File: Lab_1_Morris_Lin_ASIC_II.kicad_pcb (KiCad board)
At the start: 4 copper layers, 100 x 100 mm, 100 parts, among them IC1 74CBTLV3253D,118, IC2 74CBTLV3253D,118, IC3 74CBTLV3253D,118, IC4 74CBTLV3253D,118, IC5 74CBTLV3253D,118, IC6 74CBTLV3253D,118, J1 VDDPST_External, J10 Conn_01x14, J11 Conn_01x14, J2 PMOD_A, J3 PMOD_B, J4 VDD_Qn External, J5 VDDPST External, J6 PMOD_A, J7 PMOD_B, J8 Conn_01x14, J9 Conn_01x14, Q1 BSS138, U1 TLV75710PDBV, U2 TLV75710PDBV

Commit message: blank for run
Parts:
- removed J1: VDDPST_External, Connector:Banana_Jack_2Pin
- added J12: VDDPST External, Connector:Banana_Jack_1Pin, F.Cu at (47.8, 111.1)
- added J13: GND External, Connector:Banana_Jack_1Pin, F.Cu at (47.7, 125.5)
- IC1, IC2, IC3: moved to F.Cu
- J5: value VDDPST External -> VDDRING External
- moved JP5 76.2 mm to (44.9, 53.7), turned to 0 degrees
- moved JP9 69.5 mm to (50.4, 53.7), turned to 0 degrees
- moved R5 66.3 mm to (44.6, 69.5), turned to -90 degrees
- moved JP6 64.6 mm to (45.2, 63.9), turned to 90 degrees
- moved R6 58.4 mm to (44.6, 76.2), turned to 90 degrees
- moved IC2 58.3 mm to (61.0, 60.6), turned to 180 degrees
- moved R8 49.3 mm to (49.6, 79.2), turned to 0 degrees
- moved D7 48.9 mm to (49.7, 74.8)
- moved R10 48.0 mm to (48.8, 69.5), turned to -90 degrees
- moved IC4 44.4 mm to (118.7, 60.6), turned to 180 degrees
- moved Q1 34.0 mm to (117.9, 102.3), turned to 0 degrees
- moved D6 33.2 mm to (117.5, 107.7), turned to -90 degrees
- moved JP1 30.8 mm to (50.5, 102.5)
- moved TP6 30.8 mm to (44.1, 82.3)
- moved C5 30.8 mm to (49.7, 92.9)
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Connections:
- J2 pad 12: VDDPMOD -> unconnected-(J2-Pin_12-Pad12)
- J3 pad 12: VDDPMOD -> unconnected-(J3-Pin_12-Pad12)
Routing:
- net VDDPMOD: track 0.00 -> 96.4 mm
- net VDD: track 40.6 -> 136.5 mm
- net VDDPST: track 17.0 -> 64.4 mm, vias 14 -> 18
- net Net-(JP10-A): track 0.00 -> 46.9 mm
- net VDD_Q1: track 16.8 -> 61.8 mm
- net VDD_Q3: track 17.3 -> 59.8 mm
- net VDD_Q4: track 16.4 -> 58.1 mm
- net VDD_Q2: track 17.0 -> 55.3 mm
- net /LED_Q4: track 0.00 -> 23.7 mm
- net GND: track 0.00 -> 21.1 mm, vias 0 -> 5
- net /LED_Q3: track 0.00 -> 17.9 mm
- net Net-(JP2-B): track 0.00 -> 15.9 mm
- net /SEL_b0: track 0.00 -> 13.6 mm
- net Net-(J5-Pin_1): track 0.00 -> 12.5 mm
- net /SEL_b1: track 0.00 -> 12.4 mm
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- removed copper zone on F.Cu, net Net-(J5-Pin_1)

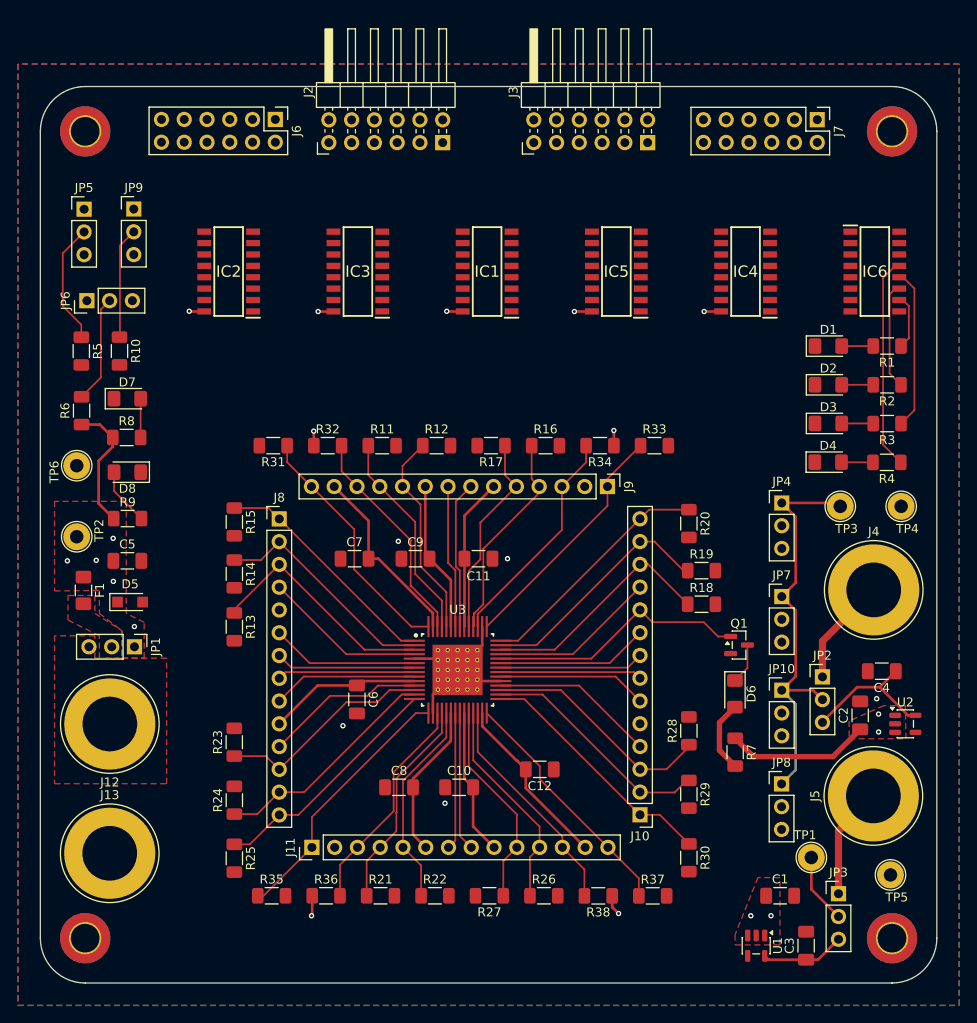
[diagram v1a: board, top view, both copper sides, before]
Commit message: Routing done, pesky GND zone error remains
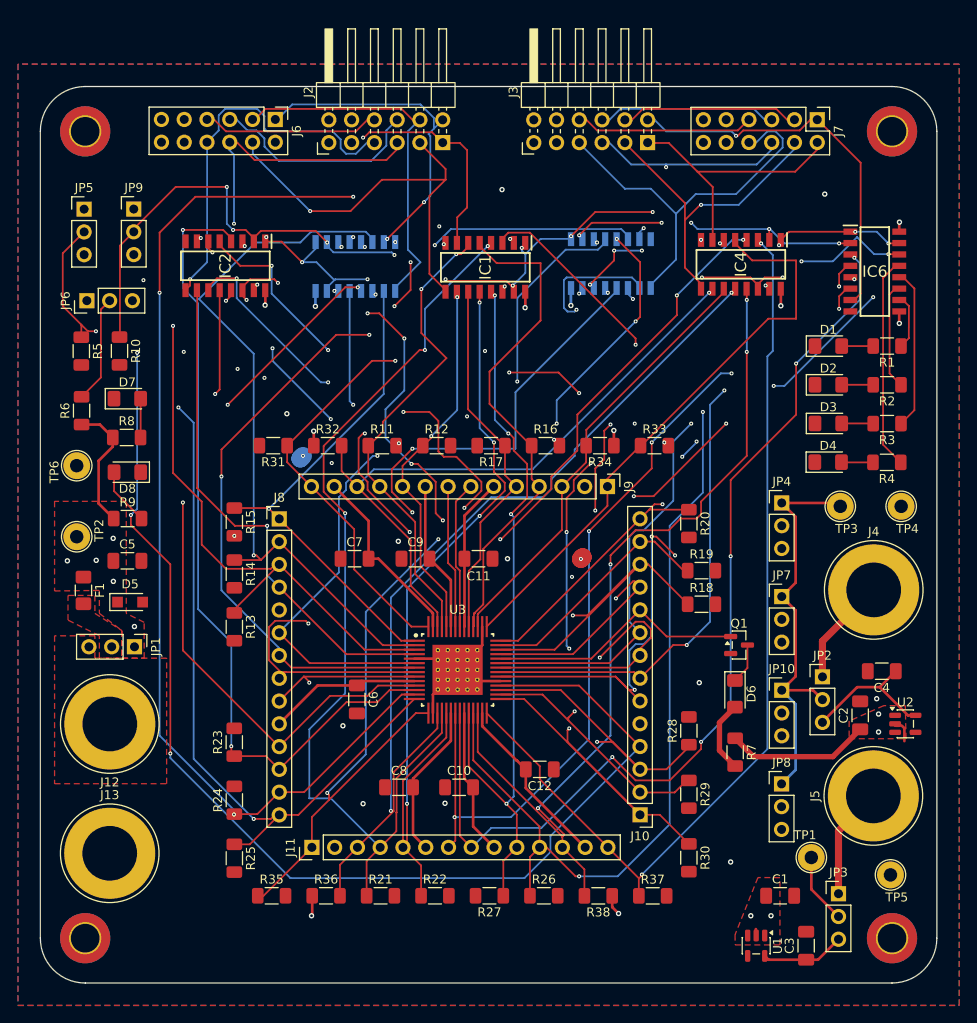
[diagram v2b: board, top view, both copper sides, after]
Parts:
- IC3, IC5: moved to B.Cu
- moved IC5 1.08 mm to (103.6, 59.8), turned to -90 degrees
- moved IC4 0.96 mm to (118.1, 59.8), turned to -90 degrees
- moved IC2 0.74 mm to (60.6, 60.0), turned to -90 degrees
- moved IC3 0.63 mm to (75.1, 60.1), turned to -90 degrees
- moved IC1 0.51 mm to (89.6, 60.2), turned to -90 degrees
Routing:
- net /~{OE}: track 12.0 -> 139.4 mm, vias 0 -> 15
- net /s_out_Q4: track 18.3 -> 145.1 mm, vias 0 -> 5
- net /SEL_b0: track 13.6 -> 126.4 mm, vias 0 -> 13
- net /Krdy_Q4: track 23.9 -> 121.4 mm, vias 0 -> 3
- net /s_in_Q3: track 25.6 -> 122.5 mm, vias 0 -> 4
- net /BSY_Q4: track 15.5 -> 110.8 mm, vias 0 -> 5
- net /SEL_b1: track 12.4 -> 106.8 mm, vias 0 -> 10
- net /CLK_Q3: track 29.5 -> 116.5 mm, vias 0 -> 5
- net /BSY_Q3: track 15.3 -> 101.3 mm, vias 0 -> 5
- net /Dvld_Q1: track 15.6 -> 99.4 mm, vias 0 -> 5
- net /Krdy_Q3: track 23.9 -> 106.8 mm, vias 0 -> 3
- net /s_update_Q4: track 25.9 -> 106.7 mm, vias 0 -> 4
- net /s_clk_Q3: track 26.8 -> 105.2 mm, vias 0 -> 4
- net /CLK_Q4: track 27.4 -> 105.5 mm, vias 0 -> 2
- net /RSTn_Q3: track 24.9 -> 102.4 mm, vias 0 -> 2
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
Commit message: Routing Attempt 2 initial
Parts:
- removed D7: ~{OE}, LED_SMD:LED_1206_3216Metric_Pad1.42x1.75mm_HandSolder
- removed J13: GND External, Connector:Banana_Jack_1Pin
- removed R8: 470, Resistor_SMD:R_1206_3216Metric_Pad1.30x1.75mm_HandSolder
- IC3, IC5: moved to F.Cu
- J12: footprint Connector:Banana_Jack_1Pin -> Connector:Banana_Jack_2Pin
- J6: value PMOD_A -> Logic_Analyzer_PMOD_A; footprint ASIC_II:PinHeader_VertNum_2x06_P2.54mm_Vertical -> ASIC_II:PinHeader_VertNum_2x05_P2.54mm_Vertical
- J7: value PMOD_B -> Logic_Analyzer_PMOD_B; footprint ASIC_II:PinHeader_VertNum_2x06_P2.54mm_Vertical -> ASIC_II:PinHeader_VertNum_2x05_P2.54mm_Vertical
- moved R6 85.1 mm to (124.8, 47.7)
- moved JP6 77.4 mm to (119.9, 43.6), turned to 0 degrees
- moved R10 70.1 mm to (115.5, 47.8)
- moved R5 65.8 mm to (106.6, 47.7)
- moved JP9 61.5 mm to (111.1, 43.7)
- moved JP5 58.2 mm to (102.2, 43.7)
- moved TP2 37.9 mm to (45.0, 128.1), turned to 0 degrees
- moved TP6 37.4 mm to (43.3, 119.7), turned to 0 degrees
- moved J7 35.9 mm to (91.5, 50.9)
- moved JP1 33.2 mm to (43.8, 70.0), turned to 0 degrees
- moved D4 30.0 mm to (135.0, 52.8), turned to 180 degrees
- moved R4 29.8 mm to (128.4, 52.8), turned to 0 degrees
- moved D3 21.7 mm to (135.0, 57.1), turned to 180 degrees
- moved R3 21.4 mm to (128.4, 57.1), turned to 0 degrees
- moved F1 17.1 mm to (48.1, 79.4), turned to 90 degrees
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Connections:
- H1 pad 1: (no net) -> unconnected-(H1-Pad1)
- H2 pad 1: (no net) -> unconnected-(H2-Pad1)_2
- H3 pad 1: (no net) -> unconnected-(H3-Pad1)_2
- H4 pad 1: (no net) -> unconnected-(H4-Pad1)_1
- J2 pad 12: unconnected-(J2-Pin_12-Pad12) -> VDDPMOD
- J3 pad 12: unconnected-(J3-Pin_12-Pad12) -> VDDPMOD
- J6 pad 10: /PMOD_A10 -> GND
- J6 pad 5: unconnected-(J6-Pin_5-Pad5) -> GND
- J6 pad 6: GND -> /PMOD_A7
- J6 pad 7: /PMOD_A7 -> /PMOD_A8
- J6 pad 8: /PMOD_A8 -> /PMOD_A9
- J6 pad 9: /PMOD_A9 -> /PMOD_A10
- J7 pad 10: /PMOD_B10 -> GND
- J7 pad 5: unconnected-(J7-Pin_5-Pad5) -> GND
- J7 pad 6: GND -> /PMOD_B7
- J7 pad 7: /PMOD_B7 -> /PMOD_B8
- J7 pad 8: /PMOD_B8 -> /PMOD_B9
- J7 pad 9: /PMOD_B9 -> /PMOD_B10
- JP5 pad 3: GND -> /PMOD_B8
- JP6 pad 3: GND -> /PMOD_B10
- JP9 pad 3: GND -> /PMOD_B9
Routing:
- net /~{OE}: track 139.4 -> 4.93 mm, vias 15 -> 0
- net /s_out_Q4: track 145.1 -> 14.6 mm, vias 5 -> 0
- net /SEL_b0: track 126.4 -> 4.43 mm, vias 13 -> 0
- net /SEL_b1: track 106.8 -> 4.43 mm, vias 10 -> 0
- net /s_in_Q3: track 122.5 -> 22.2 mm, vias 4 -> 0
- net /Krdy_Q4: track 121.4 -> 23.4 mm, vias 3 -> 0
- net /BSY_Q4: track 110.8 -> 15.1 mm, vias 5 -> 0
- net /Dvld_Q1: track 99.4 -> 12.1 mm, vias 5 -> 0
- net /CLK_Q3: track 116.5 -> 29.7 mm, vias 5 -> 0
- net /BSY_Q3: track 101.3 -> 14.6 mm, vias 5 -> 0
- net /CLK_Q4: track 105.5 -> 19.7 mm, vias 2 -> 0
- net /s_update_Q4: track 106.7 -> 21.9 mm, vias 4 -> 0
- net /Krdy_Q3: track 106.8 -> 25.4 mm, vias 3 -> 0
- net /s_clk_Q3: track 105.2 -> 24.2 mm, vias 4 -> 0
- net /s_update_Q2: track 102.6 -> 23.0 mm, vias 5 -> 0
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- added copper zone on In1.Cu, net VDDPMOD
- removed copper zone on B.Cu, net GND
- removed copper zone on F.Cu, net Net-(J12-Pin_1)
- removed copper zone on F.Cu, net Net-(JP1-C)

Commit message: Preroute again
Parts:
- moved C2 4.85 mm to (137.3, 110.3)
- moved U2 3.51 mm to (133.0, 110.7), turned to 90 degrees
- moved IC2 3.02 mm to (53.5, 65.6)
- moved IC3 2.28 mm to (66.4, 65.6)
- moved C4 1.88 mm to (135.7, 105.0), turned to 0 degrees
- moved IC1 1.70 mm to (79.4, 65.6)
- moved IC5 1.13 mm to (92.3, 65.6)
- moved TP3 0.73 mm to (128.5, 86.8)
- moved IC4 0.56 mm to (105.3, 65.6)
- turned R7 to 90 degrees
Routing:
- net /CLK_Q4: track 19.7 -> 28.0 mm
- net Net-(JP2-B): track 15.6 -> 9.95 mm
- net Net-(D6-K): track 0.00 -> 4.53 mm
- net Net-(JP10-A): track 58.4 -> 54.0 mm
- net Net-(D6-A): track 0.00 -> 3.48 mm
- net VDD: track 121.3 -> 123.2 mm
- net GND: track 24.7 -> 26.0 mm, vias 6 -> 7
- net VDDPST: track 30.5 -> 29.9 mm
- added copper zone on B.Cu, net GND

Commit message: Preroute self planned
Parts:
- moved J12 2.58 mm to (48.6, 103.7), turned to -75 degrees
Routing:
- net /PMOD_B7: track 9.13 -> 49.3 mm
- net /PMOD_B1: track 9.13 -> 29.3 mm
- net /PMOD_A1: track 9.13 -> 26.3 mm, vias 0 -> 1
- net /PMOD_B2: track 9.13 -> 25.8 mm, vias 0 -> 1
- net /PMOD_A4: track 9.13 -> 25.2 mm
- net /PMOD_A2: track 9.13 -> 22.8 mm
- net /PMOD_A7: track 9.13 -> 22.6 mm, vias 0 -> 1
- net /PMOD_B3: track 9.13 -> 22.4 mm, vias 0 -> 1
- net /PMOD_A3: track 9.13 -> 21.9 mm, vias 0 -> 1
- net /PMOD_A8: track 9.13 -> 21.2 mm, vias 0 -> 1
- net /PMOD_B4: track 9.13 -> 19.2 mm, vias 0 -> 1
- net /LED_Q2: track 9.69 -> 8.79 mm

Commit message: Routed OE and quadrant select lines
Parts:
- IC1, IC2, IC4: moved to B.Cu
- moved R6 18.4 mm to (106.6, 44.6), turned to -90 degrees
- moved JP6 17.7 mm to (102.2, 43.7)
- moved R10 9.85 mm to (124.8, 44.6), turned to 90 degrees
- moved R5 9.35 mm to (115.5, 44.6), turned to 90 degrees
- moved JP9 8.84 mm to (119.9, 43.6)
- moved JP5 8.84 mm to (111.1, 43.7)
- moved IC4 0.62 mm to (104.7, 65.6), turned to 0 degrees
- moved IC2 0.52 mm to (54.0, 65.6), turned to 0 degrees
- turned IC1 to 0 degrees
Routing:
- net /~{OE}: track 4.93 -> 117.0 mm, vias 0 -> 13
- net /SEL_b1: track 4.43 -> 96.8 mm, vias 0 -> 6
- net /SEL_b0: track 4.43 -> 93.8 mm, vias 0 -> 8
- net /PMOD_B10: track 49.1 -> 29.8 mm
- net /PMOD_B8: track 23.3 -> 37.2 mm, vias 0 -> 1
- net /PMOD_B9: track 35.6 -> 46.1 mm
- net /PMOD_A4: track 25.2 -> 18.6 mm
- net /PMOD_A2: track 22.8 -> 28.3 mm, vias 0 -> 1
- net /PMOD_B2: track 25.8 -> 30.7 mm, vias 1 -> 0
- net /PMOD_A1: track 26.3 -> 22.2 mm, vias 1 -> 0
- net /PMOD_A3: track 21.9 -> 25.2 mm
- net /PMOD_B1: track 29.3 -> 26.3 mm, vias 0 -> 1
- net VDDPST: track 29.9 -> 32.8 mm, vias 24 -> 23
